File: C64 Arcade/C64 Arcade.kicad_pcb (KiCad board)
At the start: 2 copper layers, 99.7 x 55.2 mm, 49 parts, among them J1 Port_1, J10 P2_FIRE3, J11 P1_FIRE1, J12 P1_FIRE2, J13 P1_FIRE3, J14 EXT_PWR, J2 Port_2, J3 DIRECTION, J4 UP, J5 RIGHT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

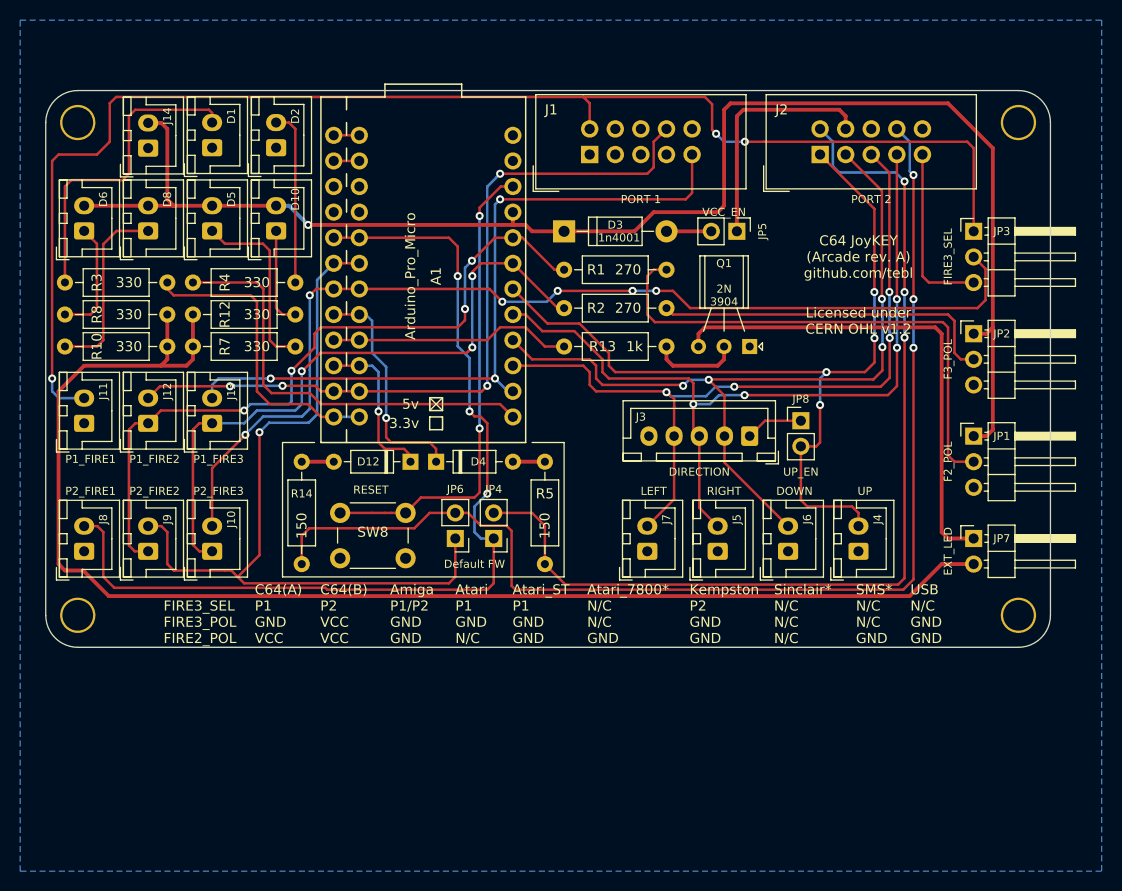
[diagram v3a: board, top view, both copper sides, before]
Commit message: New arcade layout
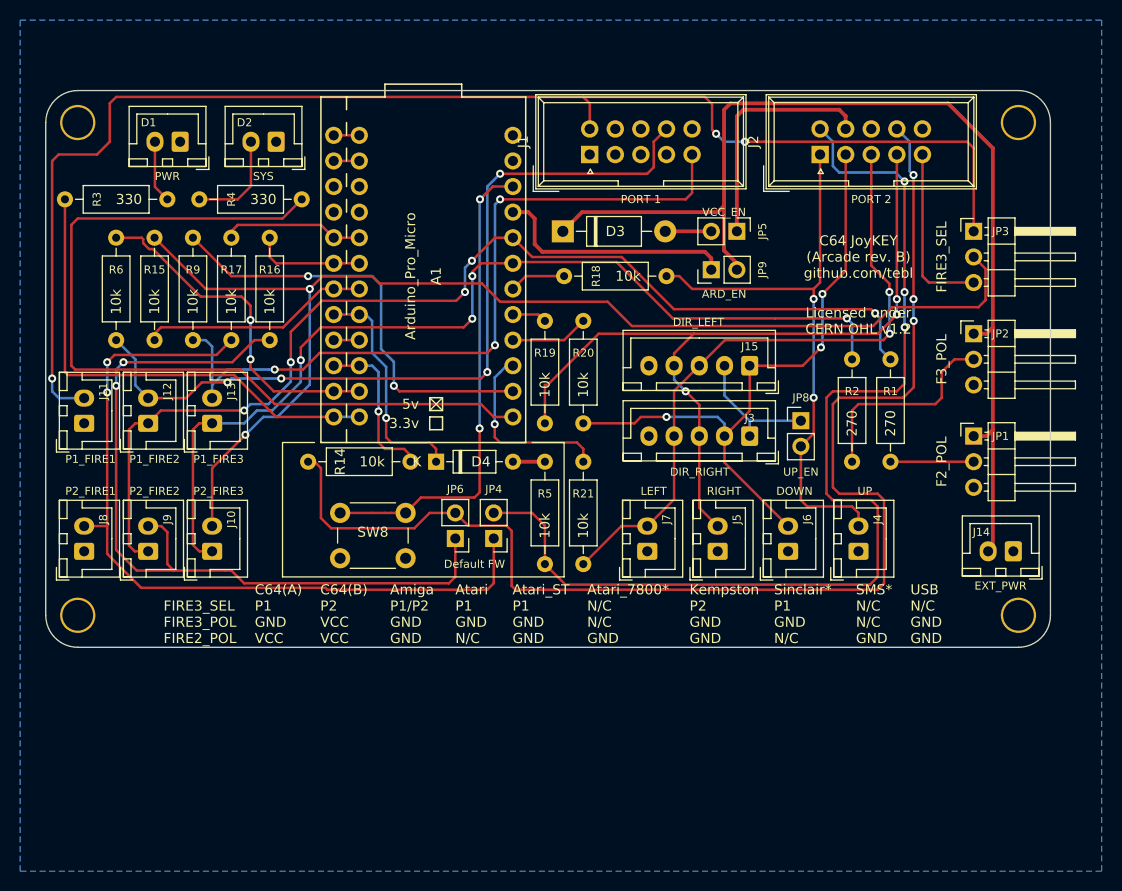
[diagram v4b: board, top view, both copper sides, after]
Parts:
- removed D10, D5, D6, D8: LED_Plugin, Connector_JST:JST_XH_B2B-XH-A_1x02_P2.50mm_Vertical
- removed D12: 1n4148, Diode_THT:D_DO-35_SOD27_P7.62mm_Horizontal
- removed JP7: EXT_LED, Connector_PinHeader_2.54mm:PinHeader_1x02_P2.54mm_Horizontal
- removed Q1: 2N3904, 2n3904:2N3904_TO-92_Horizontal_FlatSideDown
- removed R10, R12, R7, R8: 330, Resistor_THT:R_Axial_DIN0207_L6.3mm_D2.5mm_P10.16mm_Horizontal
- removed R13: 1k, Resistor_THT:R_Axial_DIN0207_L6.3mm_D2.5mm_P10.16mm_Horizontal
- added J15: DIR_LEFT, Connector_JST:JST_XH_B5B-XH-A_1x05_P2.50mm_Vertical, F.Cu at (210.8, 109.9)
- added JP9: ARD_EN, Connector_PinHeader_2.54mm:PinHeader_1x02_P2.54mm_Vertical, F.Cu at (207.0, 100.3)
- added R15: 10k, Resistor_THT:R_Axial_DIN0207_L6.3mm_D2.5mm_P10.16mm_Horizontal, F.Cu at (151.8, 107.3)
- added R16: 10k, Resistor_THT:R_Axial_DIN0207_L6.3mm_D2.5mm_P10.16mm_Horizontal, F.Cu at (163.2, 97.2)
- added R17: 10k, Resistor_THT:R_Axial_DIN0207_L6.3mm_D2.5mm_P10.16mm_Horizontal, F.Cu at (159.4, 97.2)
- added R18: 10k, Resistor_THT:R_Axial_DIN0207_L6.3mm_D2.5mm_P10.16mm_Horizontal, F.Cu at (202.6, 101.0)
- added R19: 10k, Resistor_THT:R_Axial_DIN0207_L6.3mm_D2.5mm_P10.16mm_Horizontal, F.Cu at (190.5, 115.6)
- added R20: 10k, Resistor_THT:R_Axial_DIN0207_L6.3mm_D2.5mm_P10.16mm_Horizontal, F.Cu at (194.3, 115.6)
- added R21: 10k, Resistor_THT:R_Axial_DIN0207_L6.3mm_D2.5mm_P10.16mm_Horizontal, F.Cu at (194.3, 129.5)
- added R6: 10k, Resistor_THT:R_Axial_DIN0207_L6.3mm_D2.5mm_P10.16mm_Horizontal, F.Cu at (148.0, 97.2)
- added R9: 10k, Resistor_THT:R_Axial_DIN0207_L6.3mm_D2.5mm_P10.16mm_Horizontal, F.Cu at (155.6, 107.3)
- D3: footprint Diodes_THT:D_DO-41_SOD81_P10.16mm_Horizontal -> Diode_THT:D_DO-41_SOD81_P10.16mm_Horizontal
- J3: value DIRECTION -> DIR_RIGHT
- JP1, JP2, JP3: footprint Pin_Headers:Pin_Header_Angled_1x03_Pitch2.54mm -> Connector_PinHeader_2.54mm:PinHeader_1x03_P2.54mm_Horizontal
- R14, R5: value 150 -> 10k
- SW8: footprint Buttons_Switches_THT:SW_PUSH_6mm -> Button_Switch_THT:SW_PUSH_6mm
- moved J14 94.7 mm to (237.0, 128.3), turned to 180 degrees
- moved R1 33.6 mm to (224.8, 109.2), turned to 270 degrees
- moved R2 29.0 mm to (221.0, 109.2), turned to 270 degrees
- moved R3 13.1 mm to (153.0, 93.3), turned to 180 degrees
- moved R4 12.6 mm to (156.2, 93.3), turned to 0 degrees
- moved R14 10.8 mm to (177.2, 119.4), turned to 180 degrees
- moved D1 3.23 mm to (154.3, 87.6), turned to 180 degrees
- moved D2 0.59 mm to (163.8, 87.6), turned to 180 degrees
- moved D3 0.13 mm to (192.3, 96.5)
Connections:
- net /P2_FIRE1_OUT renamed /FIRE1_OUT
- A1 pad 10: /P2_FIRE2_OUT -> /FIRE2_OUT
- A1 pad 11: P1_FIRE2 -> Net-(A1-Pad11)
- A1 pad 14: P1_FIRE3 -> Net-(A1-Pad14)
- A1 pad 15: P2_LEFT -> Net-(A1-Pad15)
- A1 pad 16: P2_DOWN -> Net-(A1-Pad16)
- A1 pad 17: P2_RIGHT -> Net-(A1-Pad17)
- A1 pad 18: P2_UP -> Net-(A1-Pad18)
- A1 pad 21: VCC -> Net-(A1-Pad21)
- J10 pad 2: /FIRE3_IN -> Net-(J10-Pad2)
- J8 pad 2: /FIRE1_IN -> Net-(J8-Pad2)
- J9 pad 2: /FIRE2_IN -> Net-(J9-Pad2)
- JP3 pad 2: /FIRE3_IN -> Net-(J10-Pad2)
- JP4 pad 1: /FIRE1_IN -> Net-(J8-Pad2)
- JP6 pad 1: /FIRE2_IN -> Net-(J9-Pad2)
- R14 pad 1: Net-(D12-Pad2) -> /FIRE2_OUT
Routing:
- net Net-(JP7-Pad2): track 135.0 -> 0.00 mm
- net Net-(J10-Pad2): track 0.00 -> 121.3 mm, vias 0 -> 2
- net /FIRE1_IN: track 95.8 -> 14.1 mm, vias 3 -> 0
- net /FIRE3_IN: track 103.3 -> 22.8 mm, vias 6 -> 0
- net Net-(J9-Pad2): track 0.00 -> 79.7 mm, vias 0 -> 2
- net Net-(J8-Pad2): track 0.00 -> 79.1 mm, vias 0 -> 2
- net /FIRE2_IN: track 78.7 -> 11.1 mm, vias 1 -> 0
- net Net-(JP7-Pad1): track 49.0 -> 0.00 mm
- net Net-(JP1-Pad2): track 51.9 -> 8.52 mm
- net Net-(A1-Pad14): track 0.00 -> 43.2 mm, vias 0 -> 2
- net VCC: track 148.1 -> 106.9 mm, vias 1 -> 0
- net /SYS: track 42.9 -> 83.8 mm
- net FIRE2_POL: track 71.7 -> 108.2 mm, vias 4 -> 5
- net Net-(A1-Pad11): track 0.00 -> 34.3 mm, vias 0 -> 2
- net FIRE3_POL: track 65.4 -> 96.7 mm, vias 3 -> 4
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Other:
- board text added: "ARD_EN"
- board text added: "C64 JoyKEY (Arcade rev. B) github.com/tebl"
- board text added: "EXT_PWR"
- board text added: "LEFT STICK"
- board text added: "RIGHT STICK"
- board text added: "Sinclair* P1 GND N/C"
- board text removed: "C64 JoyKEY (Arcade rev. A) github.com/tebl"
- board text removed: "DIRECTION"
- board text removed: "ENABLE"
- board text removed: "KEY LED"
- board text removed: "LED"
- board text removed: "Sinclair* N/C N/C N/C"
